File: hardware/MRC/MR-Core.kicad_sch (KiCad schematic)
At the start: 8 parts, among them J1 Conn_Coaxial, J16 Conn_Coaxial, J17 Conn_Coaxial, J18 Conn_Coaxial, J2 Conn_Coaxial, J3 Conn_Coaxial, J4 Conn_Coaxial, J8 Conn_Coaxial

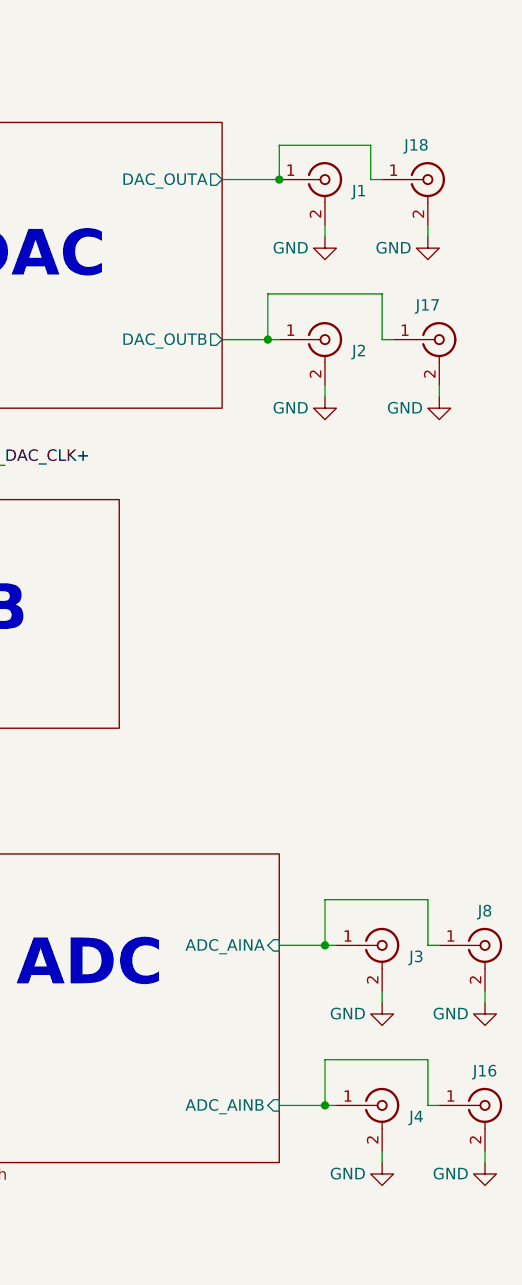
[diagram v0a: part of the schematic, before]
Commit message: Update KiCAD Version, Integrate Libraries
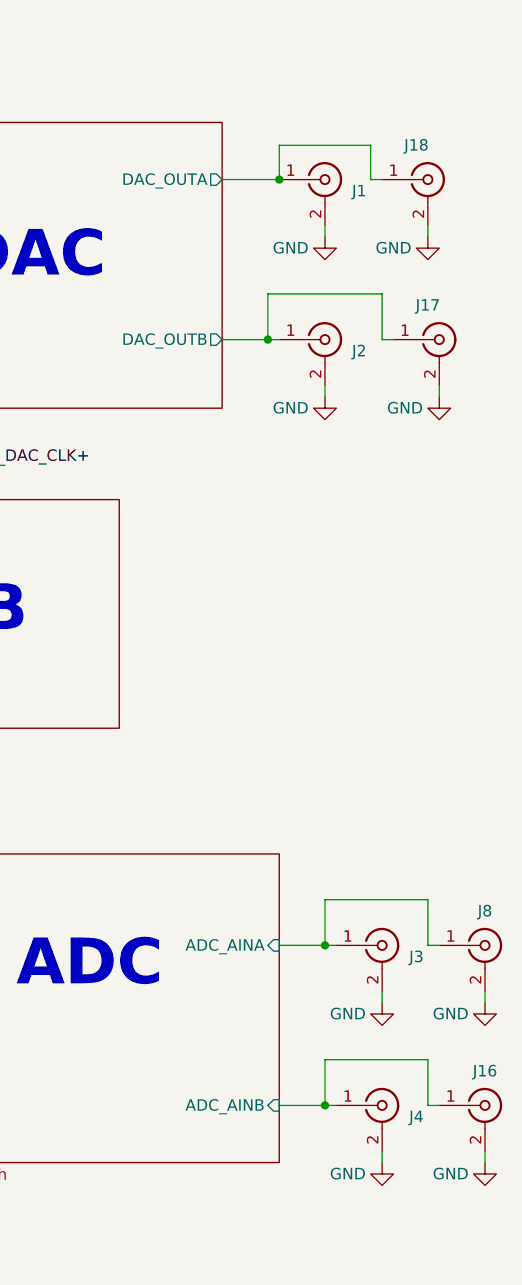
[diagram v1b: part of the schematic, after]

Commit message: Clean bill of materials
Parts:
- J16, J17, J18, J8: MPN 73415-1471 -> CONSMA013.062-G
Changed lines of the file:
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@@
 			)
 		)
-		(property "Datasheet" " ~"
+		(property "Datasheet" "~"
 			(at 248.92 160.02 0)
 			(effects
@@
 			)
 		)
-		(property "Datasheet" " ~"
+		(property "Datasheet" "~"
 			(at 242.57 74.93 0)
 			(effects
@@
 			)
 		)
-		(property "Datasheet" " ~"
+		(property "Datasheet" "~"
 			(at 260.35 160.02 0)
 			(effects
@@
 			)
 		)
-		(property "MPN" "73415-1471"
+		(property "MPN" "CONSMA013.062-G "
 			(at 260.35 160.02 0)
 			(effects
@@
 			)
 		)
-		(property "Datasheet" " ~"
+		(property "Datasheet" "~"
 			(at 254 57.15 0)
 			(effects
@@
 			)
 		)
-		(property "MPN" "73415-1471"
+		(property "MPN" "CONSMA013.062-G "
 			(at 254 57.15 0)
 			(effects
@@
 			)
 		)
-		(property "Datasheet" " ~"
+		(property "Datasheet" "~"
 			(at 248.92 142.24 0)
 			(effects
@@
 			)
 		)
-		(property "Datasheet" " ~"
+		(property "Datasheet" "~"
 			(at 242.57 57.15 0)
 			(effects
@@
 			)
 		)
-		(property "Datasheet" " ~"
+		(property "Datasheet" "~"
 			(at 260.35 142.24 0)
 			(effects
@@
 			)
 		)
-		(property "MPN" "73415-1471"
+		(property "MPN" "CONSMA013.062-G "
 			(at 260.35 142.24 0)
 			(effects
@@
 			)
 		)
-		(property "Datasheet" " ~"
+		(property "Datasheet" "~"
 			(at 255.27 74.93 0)
 			(effects
@@
 			)
 		)
-		(property "MPN" "73415-1471"
+		(property "MPN" "CONSMA013.062-G "
 			(at 255.27 74.93 0)
 			(effects
